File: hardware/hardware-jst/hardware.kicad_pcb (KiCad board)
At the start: 2 copper layers, 123.4 x 109.1 mm, 81 parts, among them J2 Barrel_Jack, M1 Stepper_Motor_unipolar_5pin, M10 Stepper_Motor_unipolar_5pin, M11 Stepper_Motor_unipolar_5pin, M12 Stepper_Motor_unipolar_5pin, M13 Stepper_Motor_unipolar_5pin, M14 Stepper_Motor_unipolar_5pin, M2 Stepper_Motor_unipolar_5pin, M3 Stepper_Motor_unipolar_5pin, M4 Stepper_Motor_unipolar_5pin, M5 Stepper_Motor_unipolar_5pin, M6 Stepper_Motor_unipolar_5pin, M7 Stepper_Motor_unipolar_5pin, M8 Stepper_Motor_unipolar_5pin, M9 Stepper_Motor_unipolar_5pin, SW1 SW_Push_SPDT, SW10 SW_Push_SPDT, SW11 SW_Push_SPDT, SW12 SW_Push_SPDT, SW13 SW_Push_SPDT, SW14 SW_Push_SPDT, SW15 SW_Push_SPDT, SW16 SW_Push_SPDT, SW2 SW_Push_SPDT, SW3 SW_Push_SPDT, SW4 SW_Push_SPDT, SW5 SW_Push_SPDT, SW6 SW_Push_SPDT, SW7 SW_Push_SPDT, SW8 SW_Push_SPDT, SW9 SW_Push_SPDT, U1 WeMos_D1_mini, U10 ULN2003A, U11 ULN2003A, U12 ULN2003A, U13 ULN2003A, U14 ULN2003A, U15 ULN2003A, U16 ULN2003A, U17 ULN2003A, U2 CD4051B, U3 CD4051B, U4 ULN2003A, U5 ULN2003A, U6 ULN2003A, U7 ULN2003A, U8 ULN2003A, U9 ULN2003A

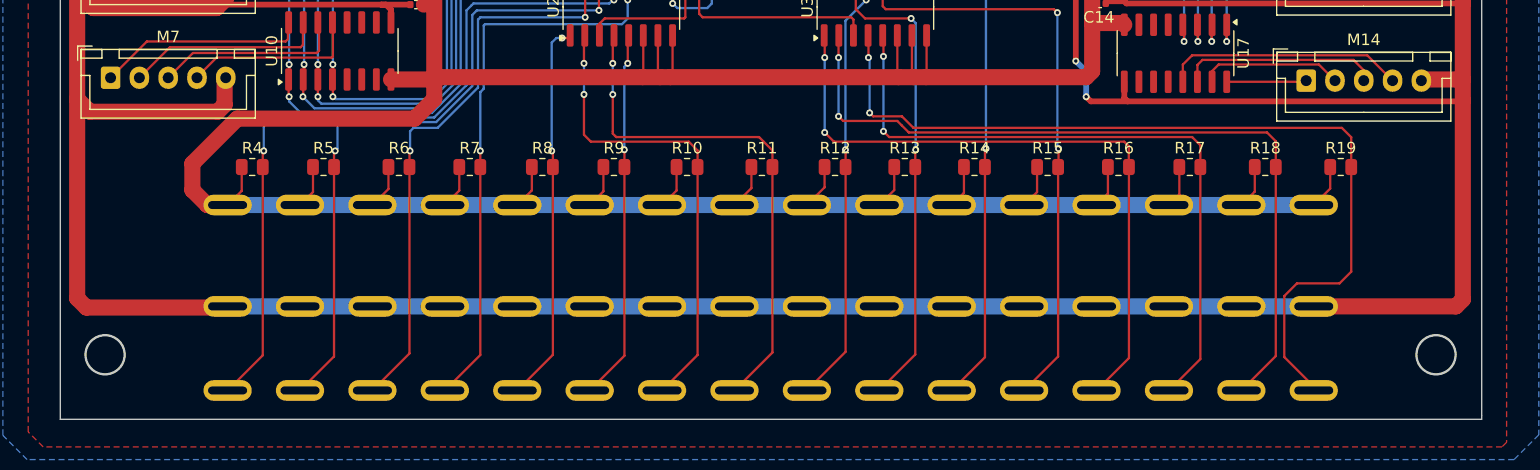
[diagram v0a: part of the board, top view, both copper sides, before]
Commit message: rotated switches on jst edition
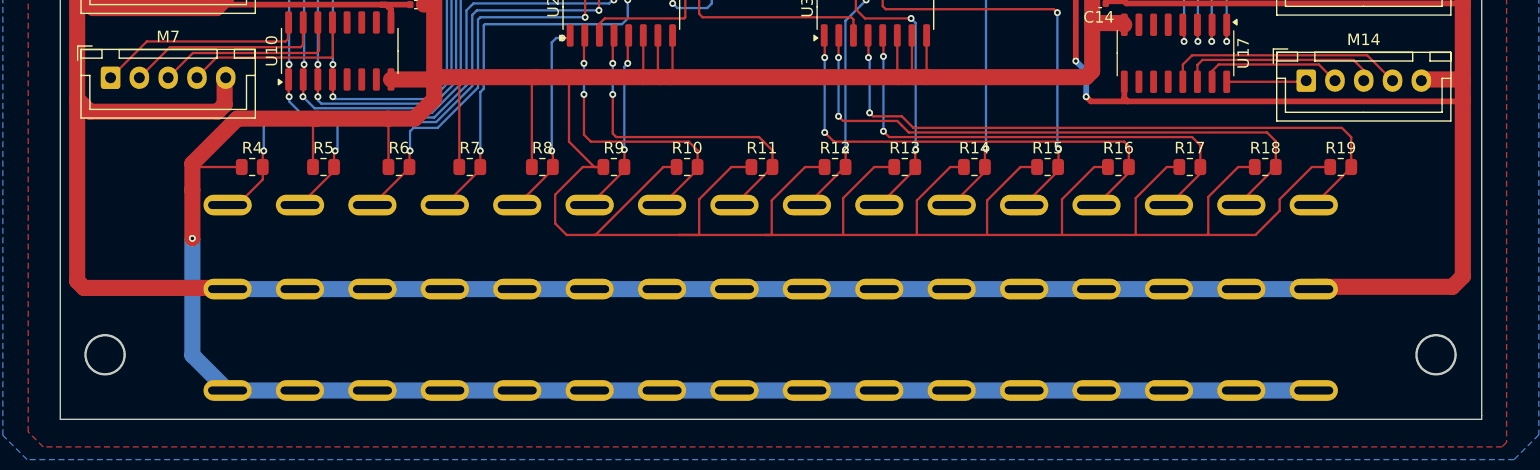
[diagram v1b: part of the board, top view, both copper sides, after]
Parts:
- moved SW1 16.1 mm to (172.5, 150.1), turned to 90 degrees
- moved SW10 16.1 mm to (229.0, 150.1), turned to 90 degrees
- moved SW11 16.1 mm to (235.3, 150.1), turned to 90 degrees
- moved SW12 16.1 mm to (241.6, 150.1), turned to 90 degrees
- moved SW13 16.1 mm to (247.9, 150.1), turned to 90 degrees
- moved SW14 16.1 mm to (254.2, 150.1), turned to 90 degrees
- moved SW15 16.1 mm to (260.5, 150.1), turned to 90 degrees
- moved SW16 16.1 mm to (266.8, 150.1), turned to 90 degrees
- moved SW2 16.1 mm to (178.7, 150.1), turned to 90 degrees
- moved SW3 16.1 mm to (185.0, 150.1), turned to 90 degrees
- moved SW4 16.1 mm to (191.3, 150.1), turned to 90 degrees
- moved SW5 16.1 mm to (197.6, 150.1), turned to 90 degrees
- moved SW6 16.1 mm to (203.9, 150.1), turned to 90 degrees
- moved SW7 16.1 mm to (210.2, 150.1), turned to 90 degrees
- moved SW8 16.1 mm to (216.5, 150.1), turned to 90 degrees
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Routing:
- net GND: track 588.9 -> 739.7 mm, vias 0 -> 1
- net SW16: track 77.1 -> 56.7 mm
- net SW2: track 57.6 -> 41.5 mm
- net SW7: track 41.2 -> 25.1 mm
- net SW15: track 68.8 -> 52.7 mm
- net SW10: track 41.7 -> 25.6 mm
- net SW6: track 32.2 -> 16.1 mm
- net SW5: track 33.4 -> 17.3 mm
- net SW4: track 49.4 -> 33.3 mm
- net SW3: track 50.0 -> 33.9 mm
- net SW14: track 58.8 -> 42.7 mm
- net SW13: track 57.7 -> 41.6 mm
- net SW12: track 51.9 -> 35.8 mm
- net SW11: track 51.8 -> 35.7 mm
- net SW8: track 45.3 -> 29.2 mm
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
